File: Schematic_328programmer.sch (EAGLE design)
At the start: 15 parts, among them IC1 ATTiny85, U1 ATMEGA328P_TQFP, Y1 16mhz

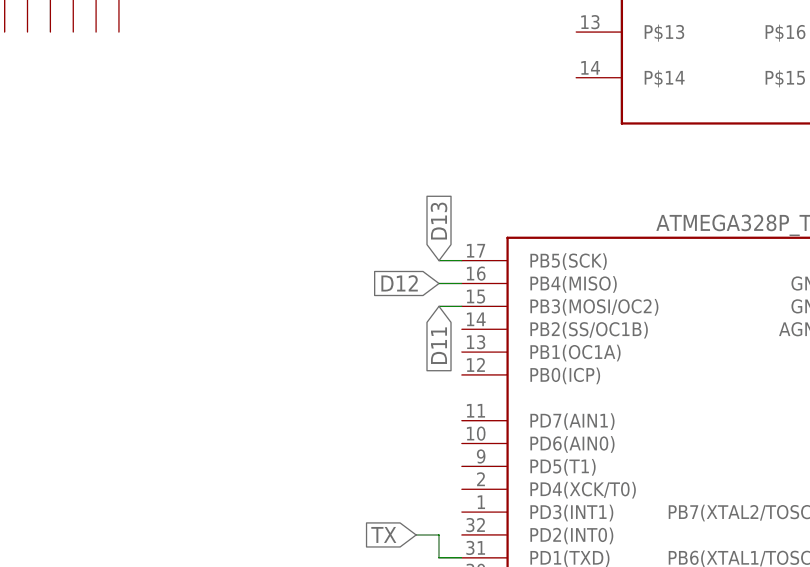
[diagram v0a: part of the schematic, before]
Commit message: Updated Board CAD files
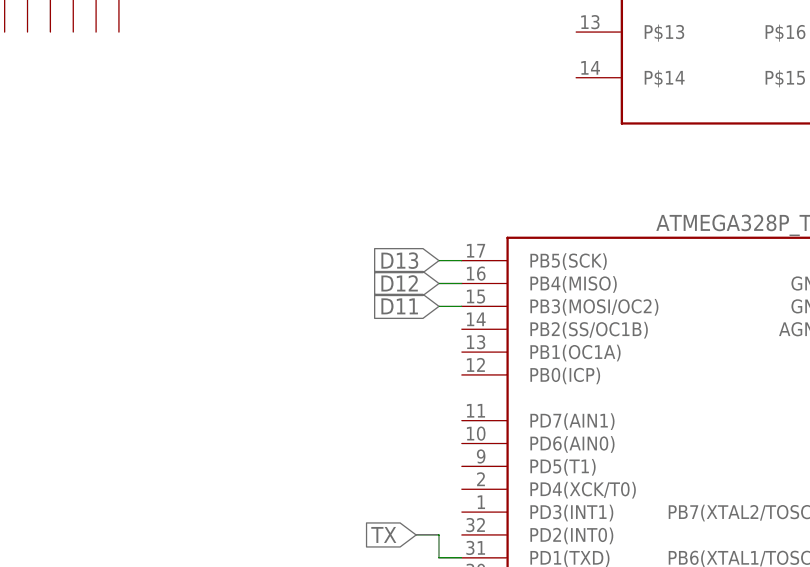
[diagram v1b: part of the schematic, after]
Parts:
- U$1: value ARDUINOUNO -> ARDUINO-NOHOLE; device adafruit:ARDUINOUNO -> adafruit:ARDUINO-NOHOLE
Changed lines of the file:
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@@
 <grid distance="0.1" unitdist="inch" unit="inch" style="lines" multiple="1" display="no" altdistance="0.01" altunitdist="inch" altunit="inch"/>
 <layers>
-<layer number="1" name="Top" color="4" fill="1" visible="no" active="no"/>
-<layer number="16" name="Bottom" color="1" fill="1" visible="no" active="no"/>
-<layer number="17" name="Pads" color="2" fill="1" visible="no" active="no"/>
-<layer number="18" name="Vias" color="2" fill="1" visible="no" active="no"/>
-<layer number="19" name="Unrouted" color="6" fill="1" visible="no" active="no"/>
-<layer number="20" name="Dimension" color="15" fill="1" visible="no" active="no"/>
-<layer number="21" name="tPlace" color="14" fill="1" visible="no" active="no"/>
-<layer number="22" name="bPlace" color="7" fill="1" visible="no" active="no"/>
-<layer number="23" name="tOrigins" color="15" fill="1" visible="no" active="no"/>
-<layer number="24" name="bOrigins" color="15" fill="1" visible="no" active="no"/>
-<layer number="25" name="tNames" color="7" fill="1" visible="no" active="no"/>
-<layer number="26" name="bNames" color="7" fill="1" visible="no" active="no"/>
-<layer number="27" name="tValues" color="7" fill="1" visible="no" active="no"/>
-<layer number="28" name="bValues" color="7" fill="1" visible="no" active="no"/>
+<layer number="1" name="Top" color="4" fill="1" visible="yes" active="no"/>
+<layer number="16" name="Bottom" color="1" fill="1" visible="yes" active="no"/>
+<layer number="17" name="Pads" color="2" fill="1" visible="yes" active="no"/>
+<layer number="18" name="Vias" color="2" fill="1" visible="yes" active="no"/>
+<layer number="19" name="Unrouted" color="6" fill="1" visible="yes" active="no"/>
+<layer number="20" name="Dimension" color="15" fill="1" visible="yes" active="no"/>
+<layer number="21" name="tPlace" color="7" fill="1" visible="yes" active="no"/>
+<layer number="22" name="bPlace" color="7" fill="1" visible="yes" active="no"/>
+<layer number="23" name="tOrigins" color="15" fill="1" visible="yes" active="no"/>
+<layer number="24" name="bOrigins" color="15" fill="1" visible="yes" active="no"/>
+<layer number="25" name="tNames" color="7" fill="1" visible="yes" active="no"/>
+<layer number="26" name="bNames" color="7" fill="1" visible="yes" active="no"/>
+<layer number="27" name="tValues" color="7" fill="1" visible="yes" active="no"/>
+<layer number="28" name="bValues" color="7" fill="1" visible="yes" active="no"/>
 <layer number="29" name="tStop" color="7" fill="3" visible="no" active="no"/>
 <layer number="30" name="bStop" color="7" fill="6" visible="no" active="no"/>
@@
 <layer number="35" name="tGlue" color="7" fill="4" visible="no" active="no"/>
 <layer number="36" name="bGlue" color="7" fill="5" visible="no" active="no"/>
-<layer number="37" name="tTest" color="7" fill="1" visible="no" active="no"/>
-<layer number="38" name="bTest" color="7" fill="1" visible="no" active="no"/>
+<layer number="37" name="tTest" color="7" fill="1" visible="yes" active="no"/>
+<layer number="38" name="bTest" color="7" fill="1" visible="yes" active="no"/>
 <layer number="39" name="tKeepout" color="4" fill="11" visible="no" active="no"/>
 <layer number="40" name="bKeepout" color="1" fill="11" visible="no" active="no"/>
@@
 <layer number="44" name="Drills" color="7" fill="1" visible="no" active="no"/>
 <layer number="45" name="Holes" color="7" fill="1" visible="no" active="no"/>
-<layer number="46" name="Milling" color="3" fill="1" visible="no" active="no"/>
-<layer number="47" name="Measures" color="7" fill="1" visible="no" active="no"/>
-<layer number="48" name="Document" color="7" fill="1" visible="no" active="no"/>
-<layer number="49" name="Reference" color="7" fill="1" visible="no" active="no"/>
-<layer number="50" name="dxf" color="7" fill="1" visible="no" active="no"/>
-<layer number="51" name="tDocu" color="7" fill="1" visible="no" active="no"/>
-<layer number="52" name="bDocu" color="7" fill="1" visible="no" active="no"/>
-<layer number="53" name="tGND_GNDA" color="7" fill="9" visible="no" active="no"/>
-<layer number="54" name="bGND_GNDA" color="1" fill="9" visible="no" active="no"/>
-<layer number="56" name="wert" color="7" fill="1" visible="no" active="no"/>
-<layer number="57" name="tCAD" color="7" fill="1" visible="no" active="no"/>
-<layer number="59" name="tCarbon" color="7" fill="1" visible="no" active="no"/>
-<layer number="60" name="bCarbon" color="7" fill="1" visible="no" active="no"/>
+<layer number="46" name="Milling" color="3" fill="1" visible="yes" active="no"/>
+<layer number="47" name="Measures" color="7" fill="1" visible="yes" active="no"/>
+<layer number="48" name="Document" color="7" fill="1" visible="yes" active="no"/>
+<layer number="49" name="Reference" color="7" fill="1" visible="yes" active="no"/>
+<layer number="50" name="dxf" color="7" fill="1" visible="yes" active="no"/>
+<layer number="51" name="tDocu" color="7" fill="1" visible="yes" active="no"/>
+<layer number="52" name="bDocu" color="7" fill="1" visible="yes" active="no"/>
+<layer number="53" name="tGND_GNDA" color="7" fill="9" visible="yes" active="no"/>
+<layer number="54" name="bGND_GNDA" color="1" fill="9" visible="yes" active="no"/>
+<layer number="56" name="wert" color="7" fill="1" visible="yes" active="no"/>
+<layer number="57" name="tCAD" color="7" fill="1" visible="yes" active="no"/>
+<layer number="59" name="tCarbon" color="7" fill="1" visible="yes" active="no"/>
+<layer number="60" name="bCarbon" color="7" fill="1" visible="yes" active="no"/>
 <layer number="90" name="Modules" color="5" fill="1" visible="yes" active="yes"/>
 <layer number="91" name="Nets" color="2" fill="1" visible="yes" active="yes"/>
@@
 </classes>
 <parts>
-<part name="U$1" library="adafruit" deviceset="ARDUINO" device="UNO"/>
+<part name="U$1" library="adafruit" deviceset="ARDUINO" device="-NOHOLE" value="ARDUINO-NOHOLE"/>
 <part name="Y1" library="SparkFun-FreqCtrl" deviceset="CRYSTAL" device="HC49US" value="16mhz"/>
 <part name="C1" library="SparkFun-Capacitors" deviceset="CAP" device="0603-CAP" value="22pF"/>
@@
 <pinref part="U1" gate="U$1" pin="PB5(SCK)"/>
 <wire x1="127" y1="-5.08" x2="124.46" y2="-5.08" width="0.1524" layer="91"/>
-<label x="124.46" y="-5.08" size="1.778" layer="95" rot="R90" xref="yes"/>
+<label x="124.46" y="-5.08" size="1.778" layer="95" rot="R180" xref="yes"/>
 </segment>
 <segment>
@@
 <pinref part="U1" gate="U$1" pin="PB3(MOSI/OC2)"/>
 <wire x1="127" y1="-10.16" x2="124.46" y2="-10.16" width="0.1524" layer="91"/>
-<label x="124.46" y="-10.16" size="1.778" layer="95" rot="R270" xref="yes"/>
-</segment>
-<segment>
+<label x="124.46" y="-10.16" size="1.778" layer="95" rot="R180" xref="yes"/>
+</segment>
+<segment>
